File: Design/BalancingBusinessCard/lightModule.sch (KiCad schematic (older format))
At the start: 18 parts

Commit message: Cleaned up fills
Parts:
- renumbered D301 to D1, D302 to D2, D303 to D3, D304 to D4, D305 to D5, D306 to D6, D307 to D7, D308 to D8, D309 to D9, R207 to R10, R208 to R11, R209 to R12, R201 to R4, R202 to R5, R203 to R6, R204 to R7, R205 to R8, R206 to R9
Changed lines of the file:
@@
 $EndDescr
 $Comp
-L Device:LED D302
+L Device:LED D2
 U 1 1 5BCBC85A
 P 3900 2800
-F 0 "D302" V 3938 2683 50  0000 R CNN
+F 0 "D2" V 3938 2683 50  0000 R CNN
 F 1 "LED" V 3847 2683 50  0000 R CNN
 F 2 "LED_SMD:LED_0603_1608Metric" H 3900 2800 50  0001 C CNN
@@
 LED_1
 $Comp
-L power:GND #PWR0117
+L power:GND #PWR017
 U 1 1 5BCBC9E3
 P 3900 3050
-F 0 "#PWR0117" H 3900 2800 50  0001 C CNN
+F 0 "#PWR017" H 3900 2800 50  0001 C CNN
 F 1 "GND" H 3905 2877 50  0000 C CNN
 F 2 "" H 3900 3050 50  0001 C CNN
@@
 	3900 2950 3900 3050
 $Comp
-L Device:LED D303
+L Device:LED D3
 U 1 1 5BCBCA64
 P 4250 2800
-F 0 "D303" V 4288 2683 50  0000 R CNN
+F 0 "D3" V 4288 2683 50  0000 R CNN
 F 1 "LED" V 4197 2683 50  0000 R CNN
 F 2 "LED_SMD:LED_0603_1608Metric" H 4250 2800 50  0001 C CNN
@@
 LED_2
 $Comp
-L power:GND #PWR0118
+L power:GND #PWR018
 U 1 1 5BCBCA6C
 P 4250 3050
-F 0 "#PWR0118" H 4250 2800 50  0001 C CNN
+F 0 "#PWR018" H 4250 2800 50  0001 C CNN
 F 1 "GND" H 4255 2877 50  0000 C CNN
 F 2 "" H 4250 3050 50  0001 C CNN
@@
 	4250 2950 4250 3050
 $Comp
-L Device:LED D304
+L Device:LED D4
 U 1 1 5BCBCA94
 P 4600 2800
-F 0 "D304" V 4638 2683 50  0000 R CNN
+F 0 "D4" V 4638 2683 50  0000 R CNN
 F 1 "LED" V 4547 2683 50  0000 R CNN
 F 2 "LED_SMD:LED_0603_1608Metric" H 4600 2800 50  0001 C CNN
@@
 LED_3
 $Comp
-L power:GND #PWR0119
+L power:GND #PWR019
 U 1 1 5BCBCA9C
 P 4600 3050
-F 0 "#PWR0119" H 4600 2800 50  0001 C CNN
+F 0 "#PWR019" H 4600 2800 50  0001 C CNN
 F 1 "GND" H 4605 2877 50  0000 C CNN
 F 2 "" H 4600 3050 50  0001 C CNN
@@
 	4600 2950 4600 3050
 $Comp
-L Device:LED D305
+L Device:LED D5
 U 1 1 5BCBCAE0
 P 4950 2800
-F 0 "D305" V 4988 2683 50  0000 R CNN
+F 0 "D5" V 4988 2683 50  0000 R CNN
 F 1 "LED" V 4897 2683 50  0000 R CNN
 F 2 "LED_SMD:LED_0603_1608Metric" H 4950 2800 50  0001 C CNN
@@
 LED_4
 $Comp
-L power:GND #PWR0120
+L power:GND #PWR020
 U 1 1 5BCBCAE8
 P 4950 3050
-F 0 "#PWR0120" H 4950 2800 50  0001 C CNN
+F 0 "#PWR020" H 4950 2800 50  0001 C CNN
 F 1 "GND" H 4955 2877 50  0000 C CNN
 F 2 "" H 4950 3050 50  0001 C CNN
@@
 	4950 2950 4950 3050
 $Comp
-L Device:LED D306
+L Device:LED D6
 U 1 1 5BCBCB54
 P 5300 2800
-F 0 "D306" V 5338 2683 50  0000 R CNN
+F 0 "D6" V 5338 2683 50  0000 R CNN
 F 1 "LED" V 5247 2683 50  0000 R CNN
 F 2 "LED_SMD:LED_0603_1608Metric" H 5300 2800 50  0001 C CNN
@@
 LED_5
 $Comp
-L power:GND #PWR0121
+L power:GND #PWR021
 U 1 1 5BCBCB5C
 P 5300 3050
-F 0 "#PWR0121" H 5300 2800 50  0001 C CNN
+F 0 "#PWR021" H 5300 2800 50  0001 C CNN
 F 1 "GND" H 5305 2877 50  0000 C CNN
 F 2 "" H 5300 3050 50  0001 C CNN
@@
 	5300 2950 5300 3050
 $Comp
-L Device:LED D307
+L Device:LED D7
 U 1 1 5BCBCC00
 P 5650 2800
-F 0 "D307" V 5688 2683 50  0000 R CNN
+F 0 "D7" V 5688 2683 50  0000 R CNN
 F 1 "LED" V 5597 2683 50  0000 R CNN
 F 2 "LED_SMD:LED_0603_1608Metric" H 5650 2800 50  0001 C CNN
@@
 LED_6
 $Comp
-L power:GND #PWR0122
+L power:GND #PWR022
 U 1 1 5BCBCC08
 P 5650 3050
-F 0 "#PWR0122" H 5650 2800 50  0001 C CNN
+F 0 "#PWR022" H 5650 2800 50  0001 C CNN
 F 1 "GND" H 5655 2877 50  0000 C CNN
 F 2 "" H 5650 3050 50  0001 C CNN
@@
 	5650 2950 5650 3050
 $Comp
-L Device:LED D308
+L Device:LED D8
 U 1 1 5BCBCCF0
 P 6000 2800
-F 0 "D308" V 6038 2683 50  0000 R CNN
+F 0 "D8" V 6038 2683 50  0000 R CNN
 F 1 "LED" V 5947 2683 50  0000 R CNN
 F 2 "LED_SMD:LED_0603_1608Metric" H 6000 2800 50  0001 C CNN
@@
 LED_7
 $Comp
-L power:GND #PWR0123
+L power:GND #PWR023
 U 1 1 5BCBCCF8
 P 6000 3050
-F 0 "#PWR0123" H 6000 2800 50  0001 C CNN
+F 0 "#PWR023" H 6000 2800 50  0001 C CNN
 F 1 "GND" H 6005 2877 50  0000 C CNN
 F 2 "" H 6000 3050 50  0001 C CNN
@@
 	6000 2950 6000 3050
 $Comp
-L Device:LED D301
+L Device:LED D1
 U 1 1 5BCBD2AC
 P 3550 2800
-F 0 "D301" V 3588 2683 50  0000 R CNN
+F 0 "D1" V 3588 2683 50  0000 R CNN
 F 1 "LED" V 3497 2683 50  0000 R CNN
 F 2 "LED_SMD:LED_0603_1608Metric" H 3550 2800 50  0001 C CNN
@@
 LED_0
 $Comp
-L power:GND #PWR0124
+L power:GND #PWR016
 U 1 1 5BCBD2B4
 P 3550 3050
-F 0 "#PWR0124" H 3550 2800 50  0001 C CNN
+F 0 "#PWR016" H 3550 2800 50  0001 C CNN
 F 1 "GND" H 3555 2877 50  0000 C CNN
 F 2 "" H 3550 3050 50  0001 C CNN
@@
 	3550 2950 3550 3050
 $Comp
-L Device:LED D309
+L Device:LED D9
 U 1 1 5BCBD4AC
 P 6350 2800
-F 0 "D309" V 6388 2683 50  0000 R CNN
+F 0 "D9" V 6388 2683 50  0000 R CNN
 F 1 "LED" V 6297 2683 50  0000 R CNN
 F 2 "LED_SMD:LED_0603_1608Metric" H 6350 2800 50  0001 C CNN
@@
 LED_8
 $Comp
-L power:GND #PWR0125
+L power:GND #PWR024
 U 1 1 5BCBD4B4
 P 6350 3050
-F 0 "#PWR0125" H 6350 2800 50  0001 C CNN
+F 0 "#PWR024" H 6350 2800 50  0001 C CNN
 F 1 "GND" H 6355 2877 50  0000 C CNN
 F 2 "" H 6350 3050 50  0001 C CNN
@@
 	6350 2950 6350 3050
 $Comp
-L Device:R R201
+L Device:R R4
 U 1 1 5C0EA341
 P 3550 2400
-F 0 "R201" H 3620 2446 50  0000 L CNN
+F 0 "R4" H 3620 2446 50  0000 L CNN
 F 1 "150R" H 3620 2355 50  0000 L CNN
 F 2 "Resistor_SMD:R_0603_1608Metric" V 3480 2400 50  0001 C CNN
@@
 	3550 2250 3550 2200
 $Comp
-L Device:R R202
+L Device:R R5
 U 1 1 5C0EA8FF
 P 3900 2400
-F 0 "R202" H 3970 2446 50  0000 L CNN
+F 0 "R5" H 3970 2446 50  0000 L CNN
 F 1 "150R" H 3970 2355 50  0000 L CNN
 F 2 "Resistor_SMD:R_0603_1608Metric" V 3830 2400 50  0001 C CNN
@@
 $EndComp
 $Comp
-L Device:R R203
+L Device:R R6
 U 1 1 5C0EA93D
 P 4250 2400
-F 0 "R203" H 4320 2446 50  0000 L CNN
+F 0 "R6" H 4320 2446 50  0000 L CNN
 F 1 "150R" H 4320 2355 50  0000 L CNN
 F 2 "Resistor_SMD:R_0603_1608Metric" V 4180 2400 50  0001 C CNN
@@
 $EndComp
 $Comp
-L Device:R R204
+L Device:R R7
 U 1 1 5C0EA97D
 P 4600 2400
-F 0 "R204" H 4670 2446 50  0000 L CNN
+F 0 "R7" H 4670 2446 50  0000 L CNN
 F 1 "150R" H 4670 2355 50  0000 L CNN
 F 2 "Resistor_SMD:R_0603_1608Metric" V 4530 2400 50  0001 C CNN
@@
 $EndComp
 $Comp
-L Device:R R205
+L Device:R R8
 U 1 1 5C0EA9B5
 P 4950 2400
-F 0 "R205" H 5020 2446 50  0000 L CNN
+F 0 "R8" H 5020 2446 50  0000 L CNN
 F 1 "150R" H 5020 2355 50  0000 L CNN
 F 2 "Resistor_SMD:R_0603_1608Metric" V 4880 2400 50  0001 C CNN
@@
 $EndComp
 $Comp
-L Device:R R206
+L Device:R R9
 U 1 1 5C0EA9FD
 P 5300 2400
-F 0 "R206" H 5370 2446 50  0000 L CNN
+F 0 "R9" H 5370 2446 50  0000 L CNN
 F 1 "150R" H 5370 2355 50  0000 L CNN
 F 2 "Resistor_SMD:R_0603_1608Metric" V 5230 2400 50  0001 C CNN
@@
 $EndComp
 $Comp
-L Device:R R207
+L Device:R R10
 U 1 1 5C0EAA3F
 P 5650 2400
-F 0 "R207" H 5720 2446 50  0000 L CNN
+F 0 "R10" H 5720 2446 50  0000 L CNN
 F 1 "150R" H 5720 2355 50  0000 L CNN
 F 2 "Resistor_SMD:R_0603_1608Metric" V 5580 2400 50  0001 C CNN
@@
 $EndComp
 $Comp
-L Device:R R208
+L Device:R R11
 U 1 1 5C0EAA7D
 P 6000 2400
-F 0 "R208" H 6070 2446 50  0000 L CNN
+F 0 "R11" H 6070 2446 50  0000 L CNN
 F 1 "150R" H 6070 2355 50  0000 L CNN
 F 2 "Resistor_SMD:R_0603_1608Metric" V 5930 2400 50  0001 C CNN
@@
 $EndComp
 $Comp
-L Device:R R209
+L Device:R R12
 U 1 1 5C0EAAC7
 P 6350 2400
-F 0 "R209" H 6420 2446 50  0000 L CNN
+F 0 "R12" H 6420 2446 50  0000 L CNN
 F 1 "150R" H 6420 2355 50  0000 L CNN
 F 2 "Resistor_SMD:R_0603_1608Metric" V 6280 2400 50  0001 C CNN

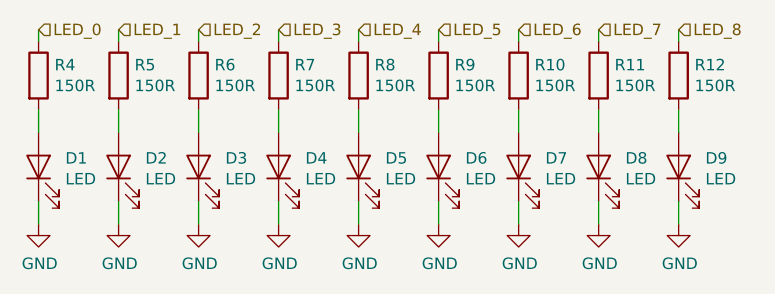
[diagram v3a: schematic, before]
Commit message: Updated resistor values
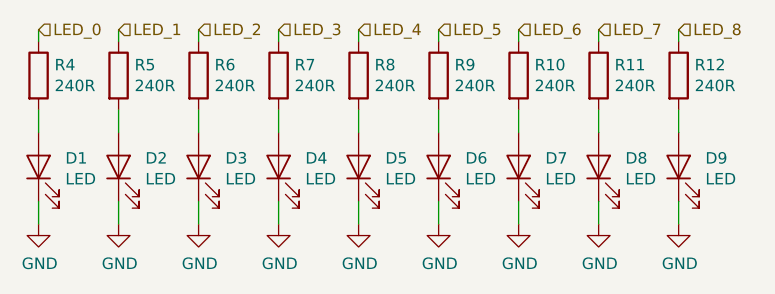
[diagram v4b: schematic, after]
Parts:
- R10, R11, R12, R4, R5, R6, R7, R8, R9: value 150R -> 240R
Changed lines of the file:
@@
 P 3550 2400
 F 0 "R4" H 3620 2446 50  0000 L CNN
-F 1 "150R" H 3620 2355 50  0000 L CNN
+F 1 "240R" H 3620 2355 50  0000 L CNN
 F 2 "Resistor_SMD:R_0603_1608Metric" V 3480 2400 50  0001 C CNN
 F 3 "~" H 3550 2400 50  0001 C CNN
@@
 P 3900 2400
 F 0 "R5" H 3970 2446 50  0000 L CNN
-F 1 "150R" H 3970 2355 50  0000 L CNN
+F 1 "240R" H 3970 2355 50  0000 L CNN
 F 2 "Resistor_SMD:R_0603_1608Metric" V 3830 2400 50  0001 C CNN
 F 3 "~" H 3900 2400 50  0001 C CNN
@@
 P 4250 2400
 F 0 "R6" H 4320 2446 50  0000 L CNN
-F 1 "150R" H 4320 2355 50  0000 L CNN
+F 1 "240R" H 4320 2355 50  0000 L CNN
 F 2 "Resistor_SMD:R_0603_1608Metric" V 4180 2400 50  0001 C CNN
 F 3 "~" H 4250 2400 50  0001 C CNN
@@
 P 4600 2400
 F 0 "R7" H 4670 2446 50  0000 L CNN
-F 1 "150R" H 4670 2355 50  0000 L CNN
+F 1 "240R" H 4670 2355 50  0000 L CNN
 F 2 "Resistor_SMD:R_0603_1608Metric" V 4530 2400 50  0001 C CNN
 F 3 "~" H 4600 2400 50  0001 C CNN
@@
 P 4950 2400
 F 0 "R8" H 5020 2446 50  0000 L CNN
-F 1 "150R" H 5020 2355 50  0000 L CNN
+F 1 "240R" H 5020 2355 50  0000 L CNN
 F 2 "Resistor_SMD:R_0603_1608Metric" V 4880 2400 50  0001 C CNN
 F 3 "~" H 4950 2400 50  0001 C CNN
@@
 P 5300 2400
 F 0 "R9" H 5370 2446 50  0000 L CNN
-F 1 "150R" H 5370 2355 50  0000 L CNN
+F 1 "240R" H 5370 2355 50  0000 L CNN
 F 2 "Resistor_SMD:R_0603_1608Metric" V 5230 2400 50  0001 C CNN
 F 3 "~" H 5300 2400 50  0001 C CNN
@@
 P 5650 2400
 F 0 "R10" H 5720 2446 50  0000 L CNN
-F 1 "150R" H 5720 2355 50  0000 L CNN
+F 1 "240R" H 5720 2355 50  0000 L CNN
 F 2 "Resistor_SMD:R_0603_1608Metric" V 5580 2400 50  0001 C CNN
 F 3 "~" H 5650 2400 50  0001 C CNN
@@
 P 6000 2400
 F 0 "R11" H 6070 2446 50  0000 L CNN
-F 1 "150R" H 6070 2355 50  0000 L CNN
+F 1 "240R" H 6070 2355 50  0000 L CNN
 F 2 "Resistor_SMD:R_0603_1608Metric" V 5930 2400 50  0001 C CNN
 F 3 "~" H 6000 2400 50  0001 C CNN
@@
 P 6350 2400
 F 0 "R12" H 6420 2446 50  0000 L CNN
-F 1 "150R" H 6420 2355 50  0000 L CNN
+F 1 "240R" H 6420 2355 50  0000 L CNN
 F 2 "Resistor_SMD:R_0603_1608Metric" V 6280 2400 50  0001 C CNN
 F 3 "~" H 6350 2400 50  0001 C CNN
